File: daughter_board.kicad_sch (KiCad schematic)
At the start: 9 parts, among them J2 Conn_02x25_Odd_Even

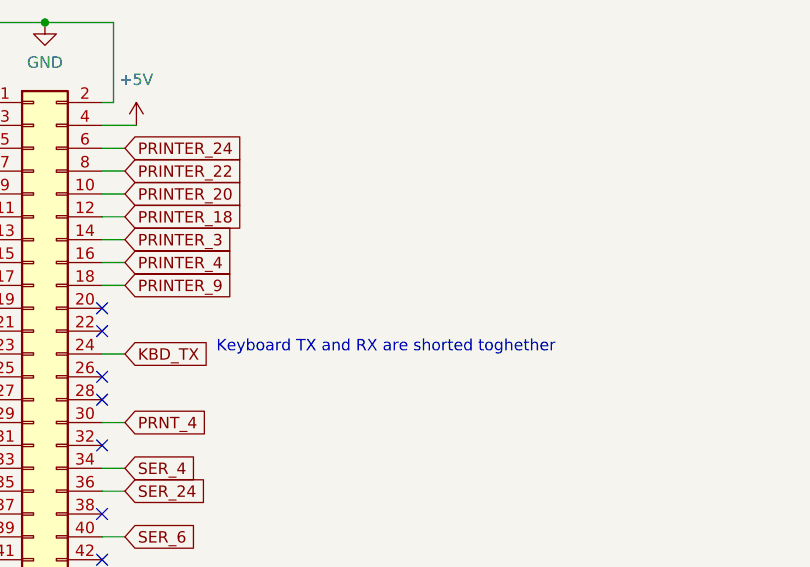
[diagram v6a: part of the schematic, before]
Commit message: pcb: added power in caps, reordered ref no, fixed power traces
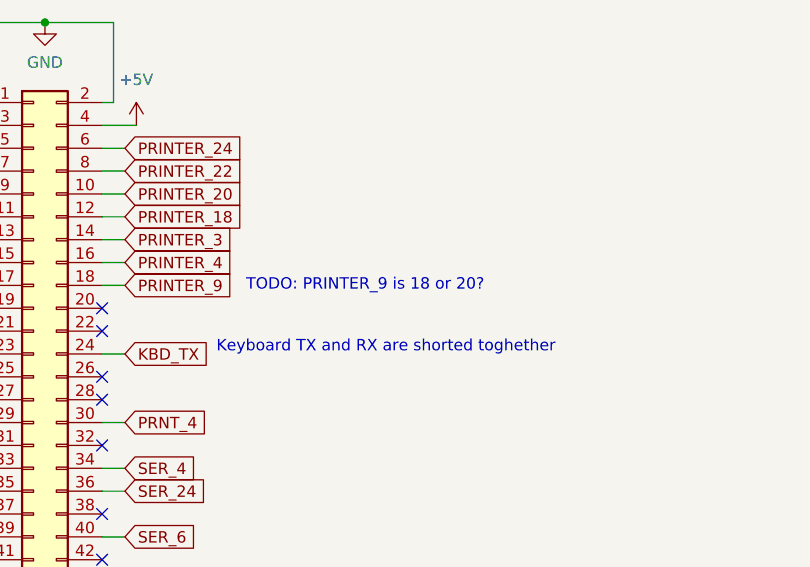
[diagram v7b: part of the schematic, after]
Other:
- note added: "TODO: PRINTER_9 is 18 or 20?"
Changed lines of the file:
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@@
+		)
+	)
+	(text "TODO: PRINTER_9 is 18 or 20?"
+		(exclude_from_sim no)
+		(at 73.152 89.662 0)
+		(effects
+			(font
+				(size 1.27 1.27)
+			)
+			(justify left bottom)
 		)
 	)
